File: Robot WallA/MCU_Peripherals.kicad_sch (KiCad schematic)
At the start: 47 parts, among them IC3 USBLC6-4SC6, IC4 USBLC6-4SC6, J2 USB4216-03-A, J3 SS-90000-009, T1 H1102NL, U7 LAN8742A, Y2 Crystal_GND24

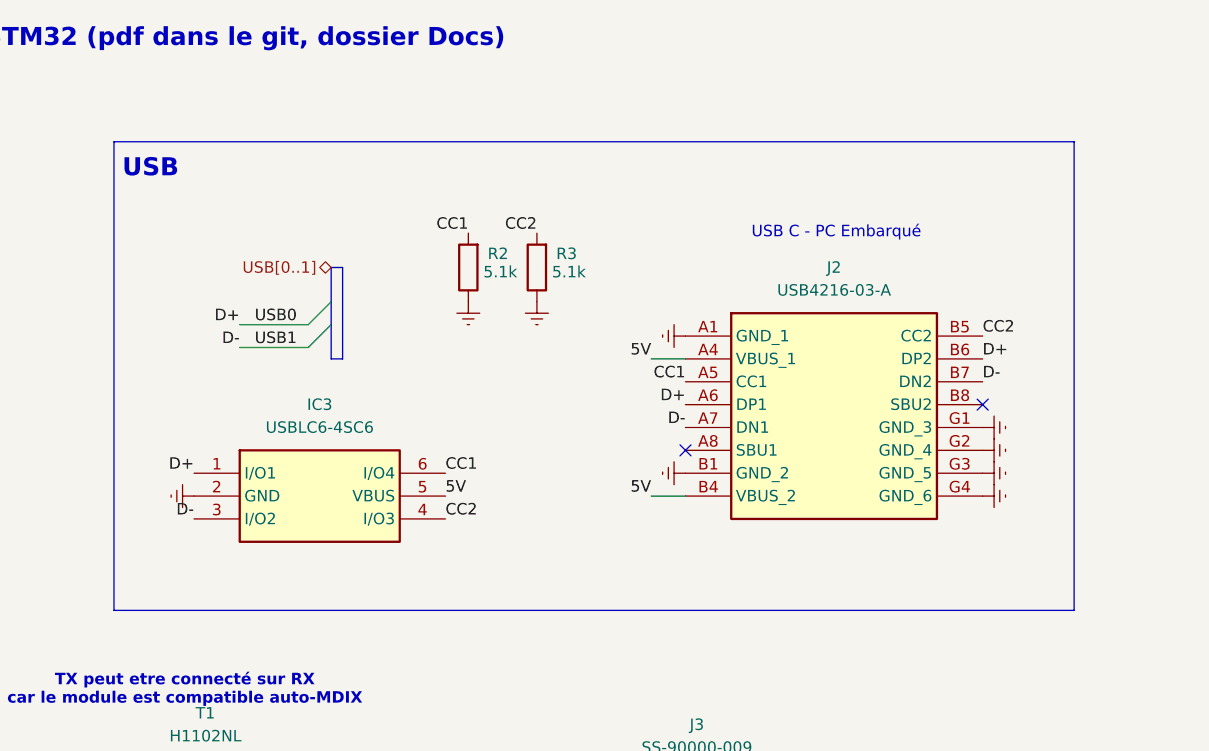
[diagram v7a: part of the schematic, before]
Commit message: Added diode for Type-C connector in case we accidentally power the board with this connector.
Updated fab files
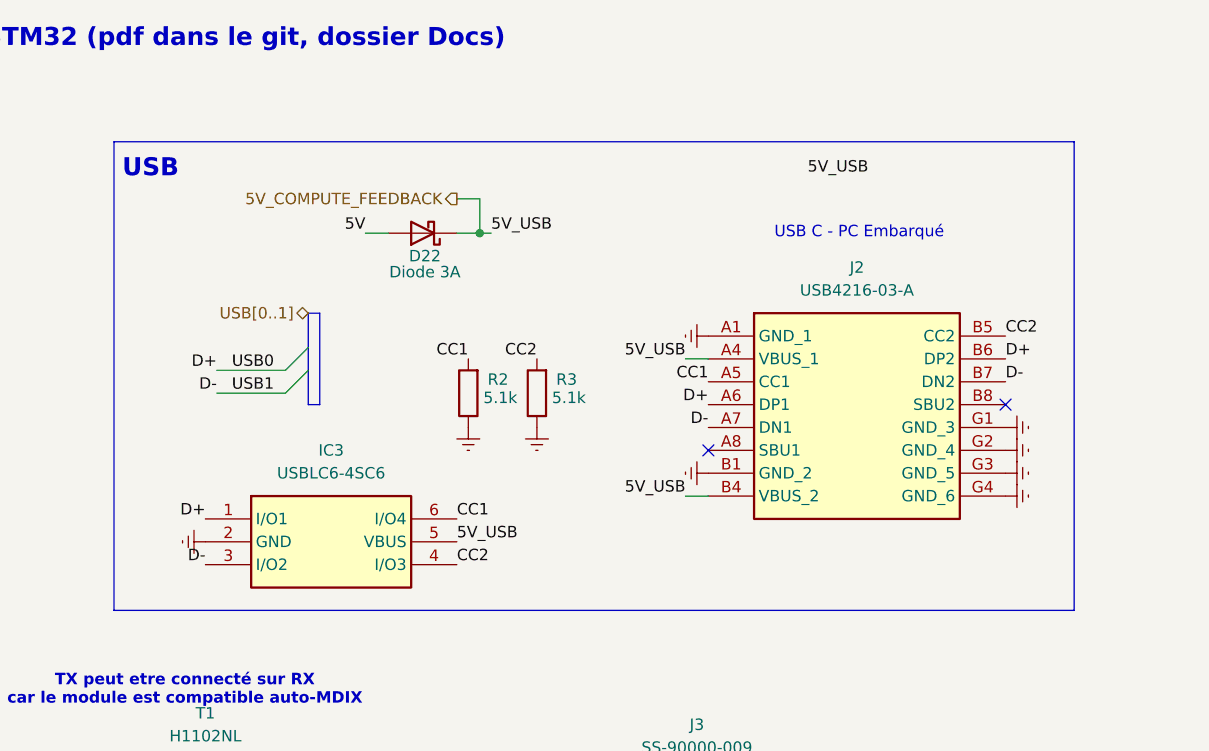
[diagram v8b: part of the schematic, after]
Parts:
- added D22: Diode 3A, Diode_SMD:D_SMP_DO-220AA, symbol Diode:SB120
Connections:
- net 5V_PC_EMBARQUE: now also D22.2 (A); no longer IC3.5 (VBUS), J2.A4 (VBUS_1), J2.B4 (VBUS_2)
- new net 5V_COMPUTE_FEEDBACK: D22.1 (K), IC3.5 (VBUS), J2.A4 (VBUS_1), J2.B4 (VBUS_2)
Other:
- moved on the sheet: IC3, J2, R2, R3
